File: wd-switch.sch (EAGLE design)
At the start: 16 parts, among them Q1 BC337, Q2 IRF530, Q3 IRF530, X1 KUSBVX

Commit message: Korrigiertes Design
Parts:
- removed Q2: IRF530, transistor-power:IRF530
- added Q4: IRL540N, n39:IRL540N
- added R3: 100R, resistor:R-EU_0207/2V
- added R4: 100K, resistor:R-EU_0207/2V
- Q3: value IRF530 -> IRL540N; device transistor-power:IRF530 -> n39:IRL540N
- R1: value 330R -> 150R
- R2: device resistor:R-EU_0207/7 -> resistor:R-EU_0207/10
- renumbered U$1 to IN, U$2 to OUT
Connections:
- new net N$11: Q1.E, R2.2, R3.2
- net GND: now also R4.2
- net N$1: now also Q4.G, R3.1, R4.1; no longer Q1.E, Q2.G, R2.2
- net N$2: now also Q3.S; no longer Q2.S
- net N$4: now also OUT.+5V, Q4.S; no longer OUT.-5V, Q3.S
- net VCC: now also IN.+5V, Q4.D; no longer IN.-5V, Q3.D
- net VDD: now also Q3.D; no longer Q2.D
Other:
- moved on the sheet: LED1, R2
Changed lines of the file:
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@@
 <part name="GND4" library="supply1" deviceset="GND" device=""/>
 <part name="SUPPLY6" library="supply2" deviceset="VCC" device=""/>
-<part name="U$1" library="n39" deviceset="PSW_5" device=""/>
+<part name="IN" library="n39" deviceset="PSW_5" device=""/>
 <part name="Q1" library="transistor-small-signal" deviceset="BC337" device=""/>
-<part name="Q2" library="transistor-power" deviceset="IRF530" device=""/>
-<part name="Q3" library="transistor-power" deviceset="IRF530" device=""/>
-<part name="GND1" library="supply1" deviceset="GND" device=""/>
 <part name="SUPPLY1" library="supply2" deviceset="VDD" device=""/>
 <part name="SUPPLY2" library="supply2" deviceset="VCC" device=""/>
 <part name="SUPPLY3" library="supply2" deviceset="VDD" device=""/>
-<part name="U$2" library="n39" deviceset="PSW_5" device=""/>
-<part name="R1" library="resistor" deviceset="R-EU_" device="0207/10" value="330R"/>
+<part name="OUT" library="n39" deviceset="PSW_5" device=""/>
+<part name="R1" library="resistor" deviceset="R-EU_" device="0207/10" value="150R"/>
 <part name="LED1" library="led" deviceset="LED" device="5MM" value="GN"/>
-<part name="R2" library="resistor" deviceset="R-EU_" device="0207/7" value="150R"/>
+<part name="R2" library="resistor" deviceset="R-EU_" device="0207/10" value="150R"/>
 <part name="GND2" library="supply1" deviceset="GND" device=""/>
 <part name="C1" library="resistor" deviceset="CPOL-EU" device="E3.5-8" value="470u"/>
@@
 <part name="SUPPLY4" library="supply2" deviceset="VCC" device=""/>
 <part name="GND5" library="supply1" deviceset="GND" device=""/>
+<part name="Q3" library="n39" deviceset="IRL540N" device=""/>
+<part name="Q4" library="n39" deviceset="IRL540N" device=""/>
+<part name="R3" library="resistor" deviceset="R-EU_" device="0207/2V" value="100R"/>
+<part name="R4" library="resistor" deviceset="R-EU_" device="0207/2V" value="100K"/>
 </parts>
 <sheets>
@@
 <instance part="GND4" gate="1" x="5.08" y="7.62"/>
 <instance part="SUPPLY6" gate="G$1" x="0" y="27.94" rot="R90"/>
-<instance part="U$1" gate="G$1" x="17.78" y="20.32" rot="R90"/>
+<instance part="IN" gate="G$1" x="17.78" y="20.32" rot="R90"/>
 <instance part="Q1" gate="1" x="55.88" y="33.02"/>
-<instance part="Q2" gate="G$1" x="76.2" y="27.94"/>
-<instance part="Q3" gate="G$1" x="91.44" y="27.94"/>
-<instance part="GND1" gate="1" x="71.12" y="-10.16"/>
 <instance part="SUPPLY1" gate="G$1" x="0" y="12.7" rot="R90"/>
 <instance part="SUPPLY2" gate="G$1" x="93.98" y="50.8"/>
 <instance part="SUPPLY3" gate="G$1" x="78.74" y="50.8"/>
-<instance part="U$2" gate="G$1" x="86.36" y="-15.24"/>
+<instance part="OUT" gate="G$1" x="86.36" y="-15.24"/>
 <instance part="R1" gate="G$1" x="50.8" y="45.72" rot="R90"/>
-<instance part="LED1" gate="G$1" x="58.42" y="-2.54"/>
-<instance part="R2" gate="G$1" x="58.42" y="7.62" rot="R90"/>
+<instance part="LED1" gate="G$1" x="58.42" y="0"/>
+<instance part="R2" gate="G$1" x="58.42" y="10.16" rot="R90"/>
 <instance part="GND2" gate="1" x="58.42" y="-12.7"/>
 <instance part="C1" gate="G$1" x="81.28" y="7.62" rot="R90"/>
@@
 <instance part="SUPPLY4" gate="G$1" x="5.08" y="55.88" rot="R90"/>
 <instance part="GND5" gate="1" x="5.08" y="45.72"/>
+<instance part="Q3" gate="IRL540N" x="78.74" y="27.94"/>
+<instance part="Q4" gate="IRL540N" x="93.98" y="27.94"/>
+<instance part="R3" gate="G$1" x="66.04" y="17.78" rot="R180"/>
+<instance part="R4" gate="G$1" x="73.66" y="10.16" rot="R270"/>
 </instances>
 <busses>
@@
 <segment>
 <pinref part="SUPPLY6" gate="G$1" pin="VCC"/>
-<pinref part="U$1" gate="G$1" pin="-5V"/>
+<pinref part="IN" gate="G$1" pin="+5V"/>
 <wire x1="2.54" y1="27.94" x2="17.78" y2="27.94" width="0.1524" layer="91"/>
 </segment>
 <segment>
 <pinref part="SUPPLY2" gate="G$1" pin="VCC"/>
-<pinref part="Q3" gate="G$1" pin="D"/>
 <wire x1="93.98" y1="48.26" x2="93.98" y2="38.1" width="0.1524" layer="91"/>
 <pinref part="Q1" gate="1" pin="C"/>
@@
 <wire x1="60.96" y1="58.42" x2="60.96" y2="38.1" width="0.1524" layer="91"/>
 <junction x="60.96" y="38.1"/>
+<pinref part="Q4" gate="IRL540N" pin="D"/>
 </segment>
 <segment>
@@
 <net name="GND" class="0">
 <segment>
-<pinref part="U$1" gate="G$1" pin="GND2"/>
+<pinref part="IN" gate="G$1" pin="GND2"/>
 <wire x1="5.08" y1="22.86" x2="17.78" y2="22.86" width="0.1524" layer="91"/>
 <pinref part="GND4" gate="1" pin="GND"/>
 <wire x1="5.08" y1="10.16" x2="5.08" y2="22.86" width="0.1524" layer="91"/>
-<pinref part="U$1" gate="G$1" pin="GND1"/>
+<pinref part="IN" gate="G$1" pin="GND1"/>
 <wire x1="17.78" y1="17.78" x2="5.08" y2="17.78" width="0.1524" layer="91"/>
 <wire x1="5.08" y1="22.86" x2="5.08" y2="17.78" width="0.1524" layer="91"/>
@@
 </segment>
 <segment>
-<pinref part="U$2" gate="G$1" pin="GND2"/>
+<pinref part="LED1" gate="G$1" pin="C"/>
+<pinref part="GND2" gate="1" pin="GND"/>
+<wire x1="58.42" y1="-5.08" x2="58.42" y2="-7.62" width="0.1524" layer="91"/>
+<pinref part="OUT" gate="G$1" pin="GND2"/>
+<wire x1="58.42" y1="-7.62" x2="58.42" y2="-10.16" width="0.1524" layer="91"/>
 <wire x1="88.9" y1="-15.24" x2="88.9" y2="-7.62" width="0.1524" layer="91"/>
-<pinref part="GND1" gate="1" pin="GND"/>
 <wire x1="88.9" y1="-7.62" x2="86.36" y2="-7.62" width="0.1524" layer="91"/>
-<pinref part="U$2" gate="G$1" pin="GND1"/>
+<pinref part="OUT" gate="G$1" pin="GND1"/>
 <wire x1="86.36" y1="-7.62" x2="83.82" y2="-7.62" width="0.1524" layer="91"/>
-<wire x1="83.82" y1="-7.62" x2="71.12" y2="-7.62" width="0.1524" layer="91"/>
+<wire x1="83.82" y1="-7.62" x2="73.66" y2="-7.62" width="0.1524" layer="91"/>
 <wire x1="83.82" y1="-15.24" x2="83.82" y2="-7.62" width="0.1524" layer="91"/>
 <junction x="83.82" y="-7.62"/>
@@
 <junction x="86.36" y="0"/>
 <pinref part="C4" gate="G$1" pin="2"/>
-</segment>
-<segment>
-<pinref part="LED1" gate="G$1" pin="C"/>
-<pinref part="GND2" gate="1" pin="GND"/>
-<wire x1="58.42" y1="-7.62" x2="58.42" y2="-10.16" width="0.1524" layer="91"/>
+<pinref part="R4" gate="G$1" pin="2"/>
+<wire x1="73.66" y1="5.08" x2="73.66" y2="-7.62" width="0.1524" layer="91"/>
+<junction x="73.66" y="-7.62"/>
+<wire x1="58.42" y1="-7.62" x2="73.66" y2="-7.62" width="0.1524" layer="91"/>
+<junction x="58.42" y="-7.62"/>
 </segment>
 <segment>
@@
 <net name="N$1" class="0">
 <segment>
-<pinref part="Q2" gate="G$1" pin="G"/>
 <wire x1="73.66" y1="25.4" x2="73.66" y2="17.78" width="0.1524" layer="91"/>
-<pinref part="Q3" gate="G$1" pin="G"/>
 <wire x1="88.9" y1="25.4" x2="88.9" y2="17.78" width="0.1524" layer="91"/>
 <wire x1="88.9" y1="17.78" x2="73.66" y2="17.78" width="0.1524" layer="91"/>
-<pinref part="Q1" gate="1" pin="E"/>
-<wire x1="58.42" y1="27.94" x2="58.42" y2="17.78" width="0.1524" layer="91"/>
-<wire x1="58.42" y1="17.78" x2="73.66" y2="17.78" width="0.1524" layer="91"/>
+<pinref part="Q3" gate="IRL540N" pin="G"/>
+<pinref part="Q4" gate="IRL540N" pin="G"/>
+<pinref part="R3" gate="G$1" pin="1"/>
+<wire x1="71.12" y1="17.78" x2="73.66" y2="17.78" width="0.1524" layer="91"/>
 <junction x="73.66" y="17.78"/>
-<pinref part="R2" gate="G$1" pin="2"/>
-<wire x1="58.42" y1="12.7" x2="58.42" y2="17.78" width="0.1524" layer="91"/>
-<junction x="58.42" y="17.78"/>
+<pinref part="R4" gate="G$1" pin="1"/>
+<wire x1="73.66" y1="17.78" x2="73.66" y2="15.24" width="0.1524" layer="91"/>
 </segment>
 </net>
@@
 <segment>
 <pinref part="SUPPLY1" gate="G$1" pin="VDD"/>
-<pinref part="U$1" gate="G$1" pin="+12V"/>
+<pinref part="IN" gate="G$1" pin="+12V"/>
 <wire x1="2.54" y1="12.7" x2="17.78" y2="12.7" width="0.1524" layer="91"/>
 </segment>
 <segment>
 <pinref part="SUPPLY3" gate="G$1" pin="VDD"/>
-<pinref part="Q2" gate="G$1" pin="D"/>
 <wire x1="78.74" y1="48.26" x2="78.74" y2="33.02" width="0.1524" layer="91"/>
+<pinref part="Q3" gate="IRL540N" pin="D"/>
 </segment>
 </net>
 <net name="N$2" class="0">
 <segment>
-<pinref part="Q2" gate="G$1" pin="S"/>
-<pinref part="U$2" gate="G$1" pin="+12V"/>
+<pinref part="OUT" gate="G$1" pin="+12V"/>
 <wire x1="78.74" y1="22.86" x2="78.74" y2="7.62" width="0.1524" layer="91"/>
 <pinref part="C1" gate="G$1" pin="+"/>
@@
 <wire x1="78.74" y1="0" x2="78.74" y2="-15.24" width="0.1524" layer="91"/>
 <junction x="78.74" y="0"/>
+<pinref part="Q3" gate="IRL540N" pin="S"/>
 </segment>
 </net>
 <net name="N$4" class="0">
 <segment>
-<pinref part="Q3" gate="G$1" pin="S"/>
-<pinref part="U$2" gate="G$1" pin="-5V"/>
+<pinref part="OUT" gate="G$1" pin="+5V"/>
 <wire x1="93.98" y1="22.86" x2="93.98" y2="7.62" width="0.1524" layer="91"/>
 <pinref part="C2" gate="G$1" pin="+"/>
@@
 <wire x1="93.98" y1="0" x2="93.98" y2="-15.24" width="0.1524" layer="91"/>
 <junction x="93.98" y="0"/>
+<pinref part="Q4" gate="IRL540N" pin="S"/>
 </segment>
 </net>
@@
 <pinref part="LED1" gate="G$1" pin="A"/>
 <pinref part="R2" gate="G$1" pin="1"/>
-<wire x1="58.42" y1="0" x2="58.42" y2="2.54" width="0.1524" layer="91"/>
+<wire x1="58.42" y1="2.54" x2="58.42" y2="5.08" width="0.1524" layer="91"/>
 </segment>
 </net>
@@
 </segment>
 </net>
+<net name="N$11" class="0">
+<segment>
+<pinref part="Q1" gate="1" pin="E"/>
+<wire x1="58.42" y1="27.94" x2="58.42" y2="17.78" width="0.1524" layer="91"/>
+<pinref part="R2" gate="G$1" pin="2"/>
+<pinref part="R3" gate="G$1" pin="2"/>
+<wire x1="58.42" y1="17.78" x2="58.42" y2="15.24" width="0.1524" layer="91"/>
+<wire x1="60.96" y1="17.78" x2="58.42" y2="17.78" width="0.1524" layer="91"/>
+<junction x="58.42" y="17.78"/>
+</segment>
+</net>

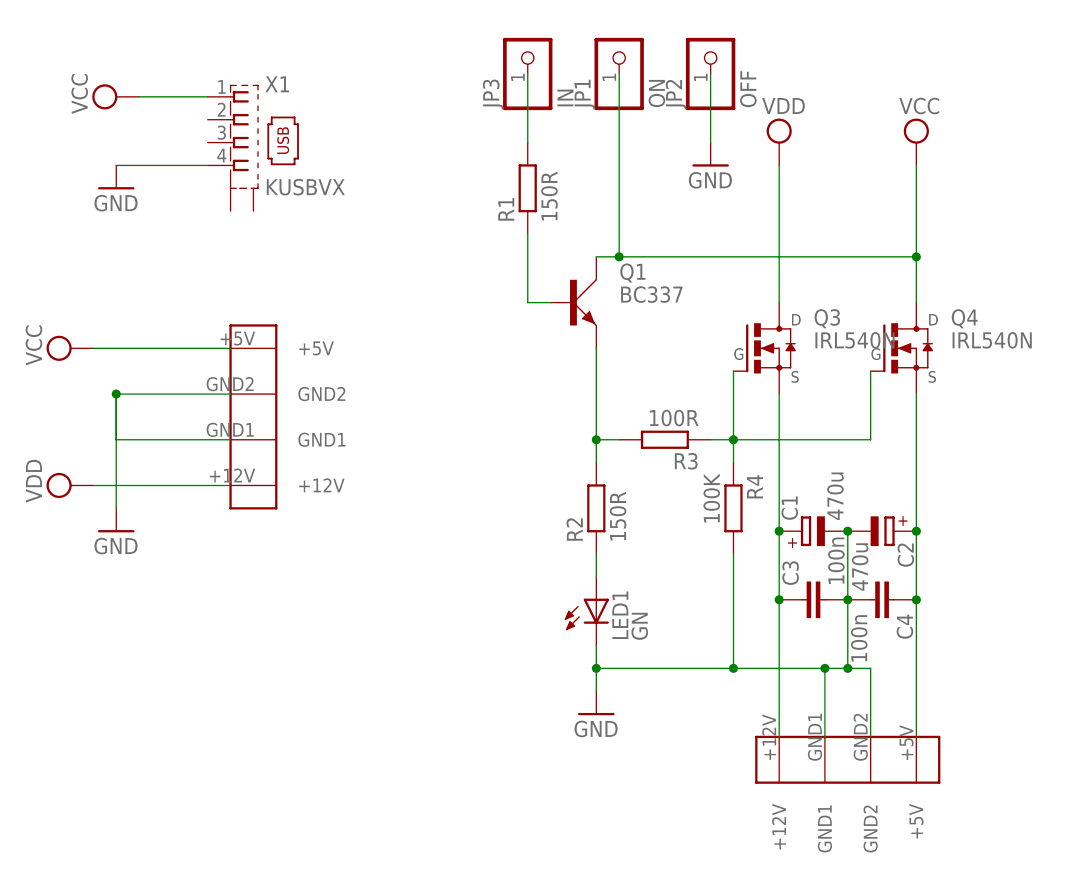
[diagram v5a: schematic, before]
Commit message: WD-Switch jetzt mit Relais
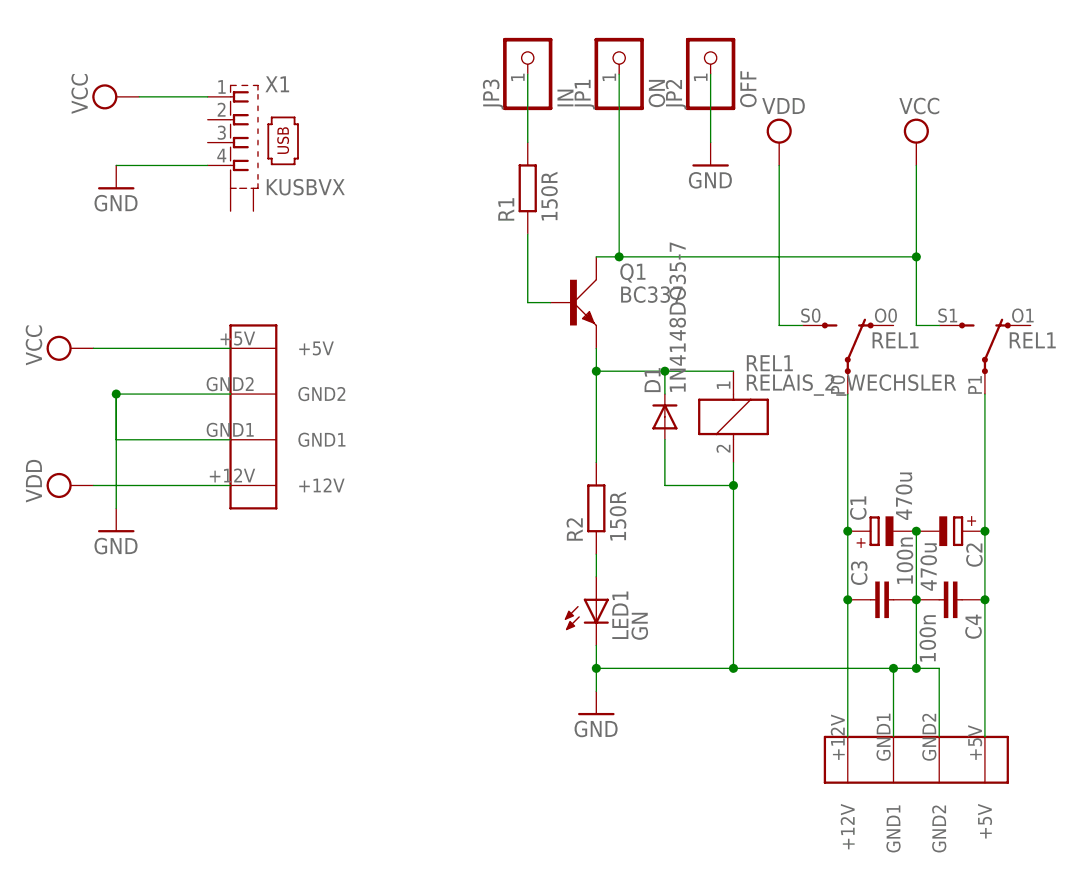
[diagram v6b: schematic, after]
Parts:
- removed Q3, Q4: IRL540N, n39:IRL540N
- removed R3: 100R, resistor:R-EU_0207/2V
- removed R4: 100K, resistor:R-EU_0207/2V
- added D1: 1N4148DO35-7, diode:1N4148DO35-7
- added REL1: RELAIS_2_WECHSLER, n39:RELAIS_2_WECHSLER
- R1: device resistor:R-EU_0207/10 -> resistor:R-EU_0207/2V
- R2: device resistor:R-EU_0207/10 -> resistor:R-EU_0207/7
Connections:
- removed net N$1: Q3.G, Q4.G, R3.1, R4.1
- net GND: now also D1.A, REL1SP.2; no longer R4.2
- net N$11: now also D1.C, REL1SP.1; no longer R3.2
- net N$2: now also REL1W1.P; no longer Q3.S
- net N$4: now also REL1W2.P; no longer Q4.S
- net VCC: now also REL1W2.S; no longer Q4.D
- net VDD: now also REL1W1.S; no longer Q3.D
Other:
- moved on the sheet: C1, C2, C3, C4
